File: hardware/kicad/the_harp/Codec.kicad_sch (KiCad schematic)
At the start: 16 parts, among them IC501 AK4621EF, U501 OPA2348AIDR

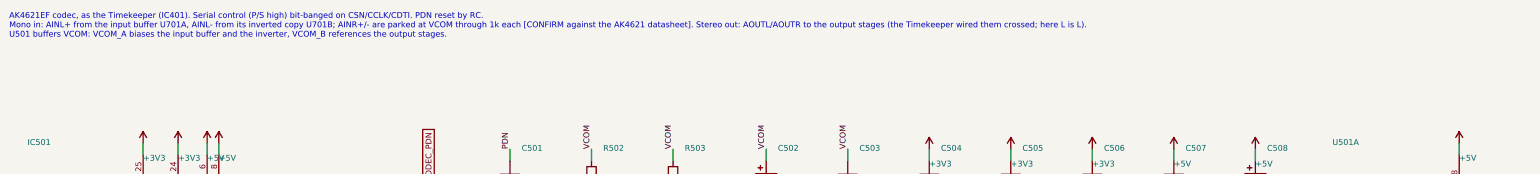
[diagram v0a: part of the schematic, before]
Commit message: Restore the THS4522 ADC driver
Reverts c744d80. The THS4522 is designed for the single 5 V analog rail
(rail-to-rail output, VOCM sets the output common mode at the codec's VCOM),
which is why the Timekeeper uses it; the OPA1656 sits at the bottom of its
supply range there. The reference leg stays tied to VCOM_A, the fix from the
Timekeeper's input noise review (H1), not left floating.

Co-Authored-By: Claude Opus 5.5 <noreply@anthropic.com>
Claude-Session: https://claude.ai/code/session_01ToUUHuo6mg178NkLtQkDLg
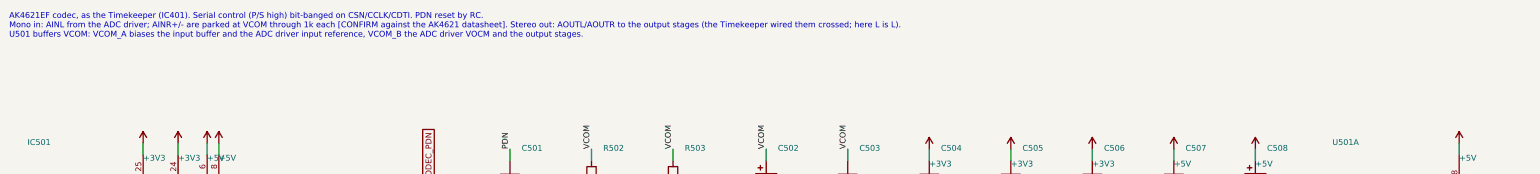
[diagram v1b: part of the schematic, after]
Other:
- note added: "AK4621EF codec, as the Timekeeper (IC401). Serial control (P/S high) bit-banged on CSN/CCLK/CDTI. PDN reset by RC. Mono in: AINL from the ADC driver; AINR+/- are parked at VCOM through 1k each [CONFIRM against the AK4621 datasheet]. Stereo out: AOUTL/AOUTR to the output stages (the Timekeeper wired them crossed; here L is L). U501 buffers VCOM: VCOM_A biases the input buffer and the ADC driver in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"
- note removed: "AK4621EF codec, as the Timekeeper (IC401). Serial control (P/S high) bit-banged on CSN/CCLK/CDTI. PDN reset by RC. Mono in: AINL+ from the input buffer U701A, AINL- from its inverted copy U701B; AINR+/- are parked at VCOM through 1k each [CONFIRM against the AK4621 datasheet]. Stereo out: AOUTL/AOUTR to the output stages (the Timekeeper wired them crossed; here L is L). U501 buffers VCOM: VCOM_A 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"
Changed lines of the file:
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@@
 		)
 	)
-	(text "AK4621EF codec, as the Timekeeper (IC401). Serial control (P/S high) bit-banged on CSN/CCLK/CDTI. PDN reset by RC.\nMono in: AINL+ from the input buffer U701A, AINL- from its inverted copy U701B; AINR+/- are parked at VCOM through 1k each [CONFIRM against the AK4621 datasheet]. Stereo out: AOUTL/AOUTR to the output stages (the Timekeeper wired them crossed; here L is L).\nU501 buffers VCOM: VCOM_A biases the input buffer and the inverter, VCOM_B references the output stages."
+	(text "AK4621EF codec, as the Timekeeper (IC401). Serial control (P/S high) bit-banged on CSN/CCLK/CDTI. PDN reset by RC.\nMono in: AINL from the ADC driver; AINR+/- are parked at VCOM through 1k each [CONFIRM against the AK4621 datasheet]. Stereo out: AOUTL/AOUTR to the output stages (the Timekeeper wired them crossed; here L is L).\nU501 buffers VCOM: VCOM_A biases the input buffer and the ADC driver input reference, VCOM_B the ADC driver VOCM and the output stages."
 		(exclude_from_sim no)
 		(at 20.32 15.24 0)

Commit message: Drop the THS4522: drive the ADC from the input OPA1656
The spare half of the input OPA1656 becomes a unity inverter about VCOM_A,
so U701A drives AINL+ and U701B drives AINL- through the THS4522 stage's
own output filter (40.2R per leg, 2.7n across, 100p to GND). Removes the
ADC Driver sheet (THS4522 and 16 passives) and, with it, the Timekeeper's
floating IN_N defect. 6 sheets, 183 parts, net check clean.

Co-Authored-By: Claude Opus 5.5 <noreply@anthropic.com>
Claude-Session: https://claude.ai/code/session_01ToUUHuo6mg178NkLtQkDLg
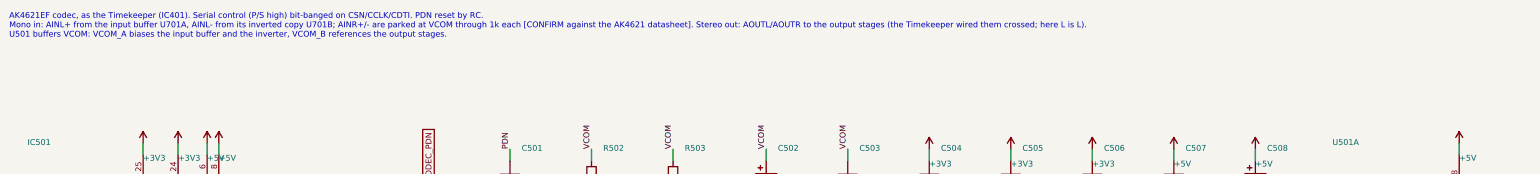
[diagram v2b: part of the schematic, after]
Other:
- note added: "AK4621EF codec, as the Timekeeper (IC401). Serial control (P/S high) bit-banged on CSN/CCLK/CDTI. PDN reset by RC. Mono in: AINL+ from the input buffer U701A, AINL- from its inverted copy U701B; AINR+/- are parked at VCOM through 1k each [CONFIRM against the AK4621 datasheet]. Stereo out: AOUTL/AOUTR to the output stages (the Timekeeper wired them crossed; here L is L). U501 buffers VCOM: VCOM_A 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"
- note removed: "AK4621EF codec, as the Timekeeper (IC401). Serial control (P/S high) bit-banged on CSN/CCLK/CDTI. PDN reset by RC. Mono in: AINL from the ADC driver; AINR+/- are parked at VCOM through 1k each [CONFIRM against the AK4621 datasheet]. Stereo out: AOUTL/AOUTR to the output stages (the Timekeeper wired them crossed; here L is L). U501 buffers VCOM: VCOM_A biases the input buffer and the ADC driver in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"
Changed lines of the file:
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@@
 		)
 	)
-	(text "AK4621EF codec, as the Timekeeper (IC401). Serial control (P/S high) bit-banged on CSN/CCLK/CDTI. PDN reset by RC.\nMono in: AINL from the ADC driver; AINR+/- are parked at VCOM through 1k each [CONFIRM against the AK4621 datasheet]. Stereo out: AOUTL/AOUTR to the output stages (the Timekeeper wired them crossed; here L is L).\nU501 buffers VCOM: VCOM_A biases the input buffer and the ADC driver input reference, VCOM_B the ADC driver VOCM and the output stages."
+	(text "AK4621EF codec, as the Timekeeper (IC401). Serial control (P/S high) bit-banged on CSN/CCLK/CDTI. PDN reset by RC.\nMono in: AINL+ from the input buffer U701A, AINL- from its inverted copy U701B; AINR+/- are parked at VCOM through 1k each [CONFIRM against the AK4621 datasheet]. Stereo out: AOUTL/AOUTR to the output stages (the Timekeeper wired them crossed; here L is L).\nU501 buffers VCOM: VCOM_A biases the input buffer and the inverter, VCOM_B references the output stages."
 		(exclude_from_sim no)
 		(at 20.32 15.24 0)
